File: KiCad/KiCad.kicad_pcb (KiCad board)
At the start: 2 copper layers, 26 parts, among them J1 DC-IN, J2 TYPE-C, SW1 TS665CJ, U1 ESP32-WROOM-32E, U2 MP1584EN, U3 CH340C, U4 RT9013-33GB

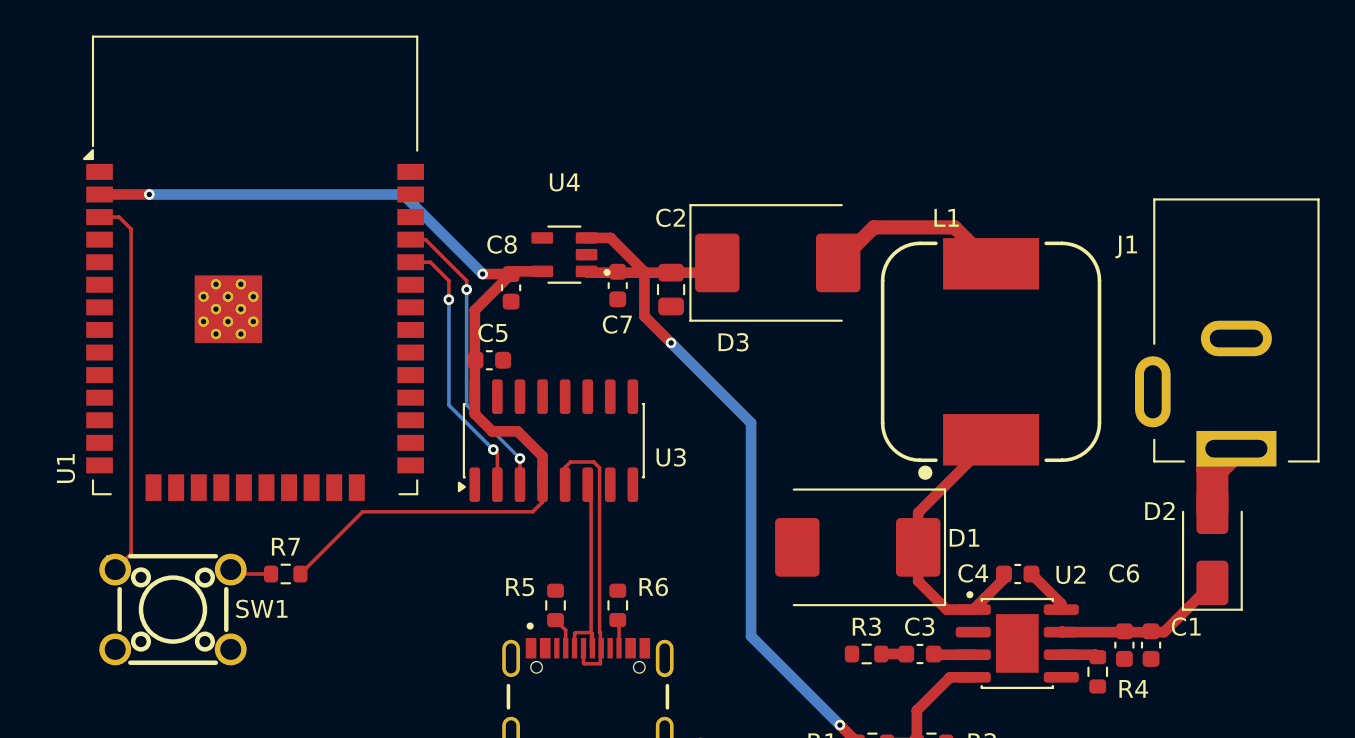
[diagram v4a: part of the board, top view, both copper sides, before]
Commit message: 完成esp32的燒錄/工作模式選擇電路之原理圖與PCB
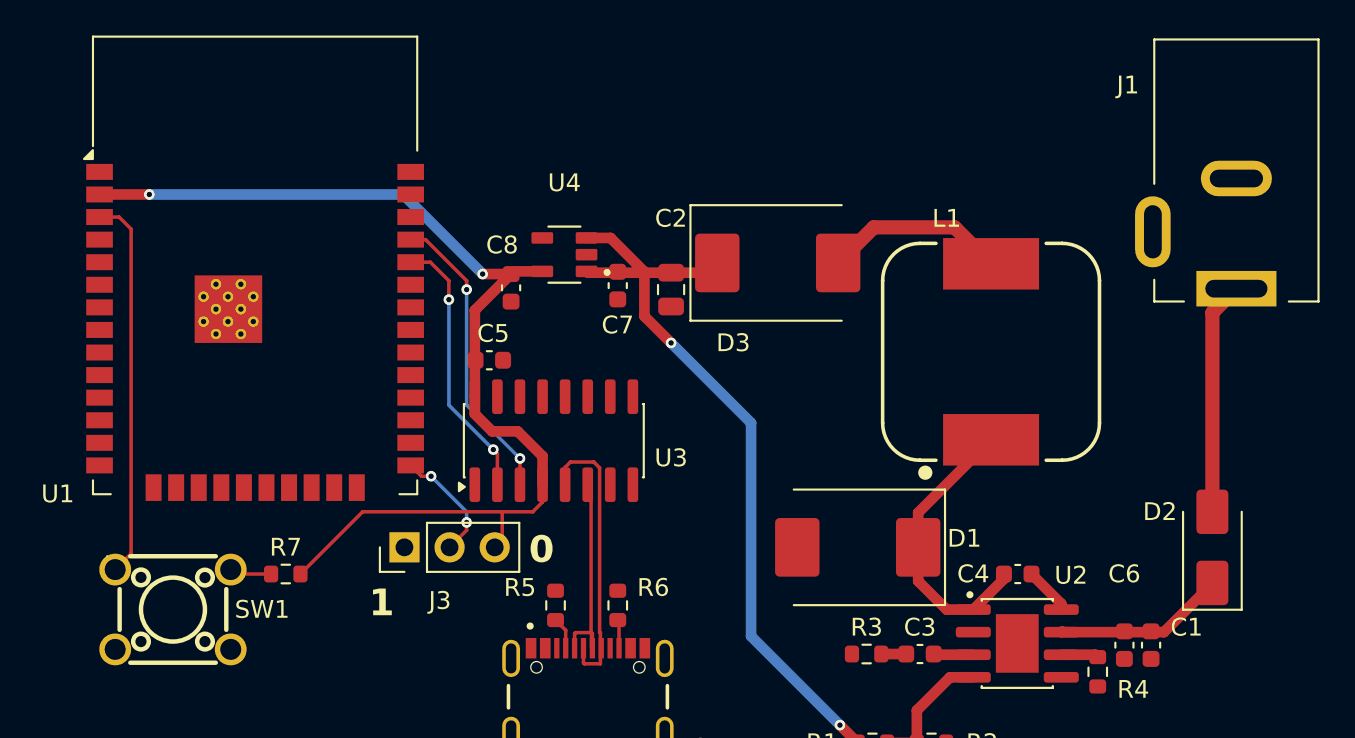
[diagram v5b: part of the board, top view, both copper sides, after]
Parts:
- added J3: Conn_01x03_Pin, Connector_PinHeader_2.54mm:PinHeader_1x03_P2.54mm_Vertical, F.Cu at (206.5, 89.0)
- moved J1 9.00 mm to (253.3, 74.5)
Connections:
- U1 pad 25: unconnected-(U1-IO0-Pad25) -> Net-(J3-Pin_2)
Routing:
- net VCC: track 4.56 -> 13.1 mm
- net Net-(J3-Pin_2): track 0.00 -> 6.63 mm, vias 0 -> 2
- net +3V3: track 57.9 -> 60.1 mm
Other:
- board text added: "0"
- board text added: "1"

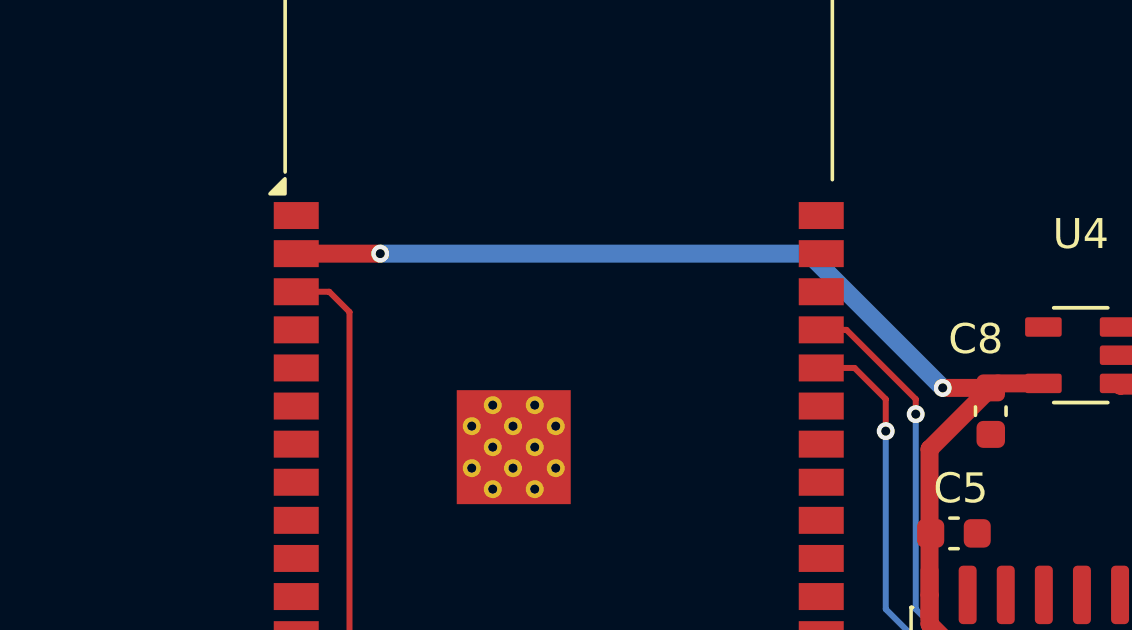
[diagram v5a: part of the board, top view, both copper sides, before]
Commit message: 補全mcu供電去偶電容
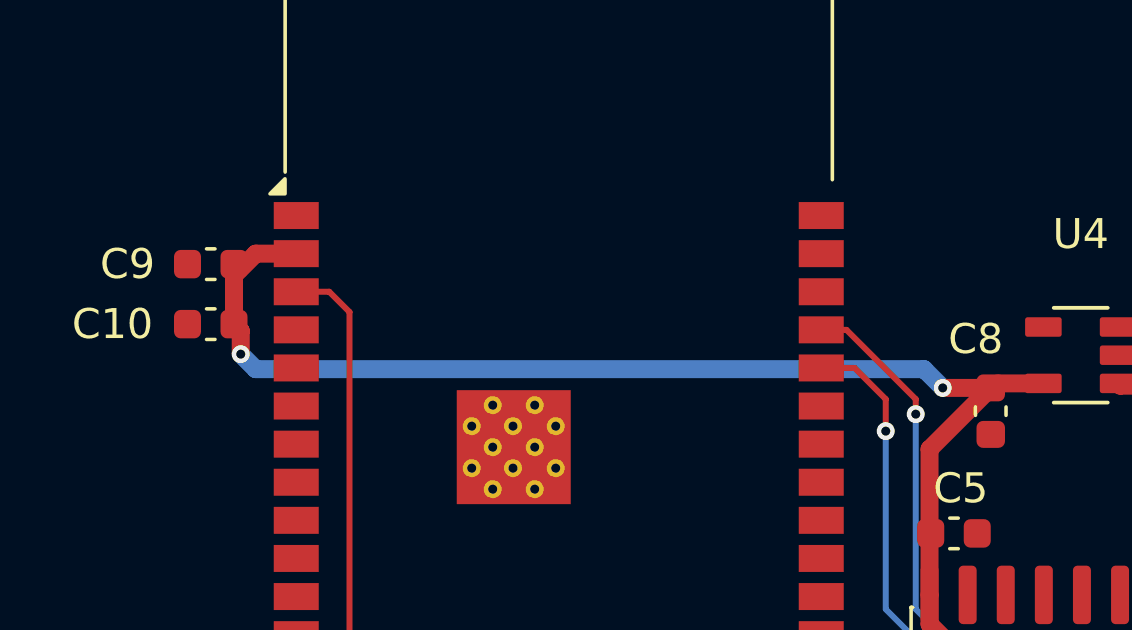
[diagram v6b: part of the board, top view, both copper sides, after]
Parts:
- added C10: 10uF, Capacitor_SMD:C_0603_1608Metric, F.Cu at (186.5, 71.5)
- added C9: 0.1uF, Capacitor_SMD:C_0603_1608Metric, F.Cu at (186.5, 69.5)
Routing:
- net +3V3: track 60.1 -> 65.6 mm

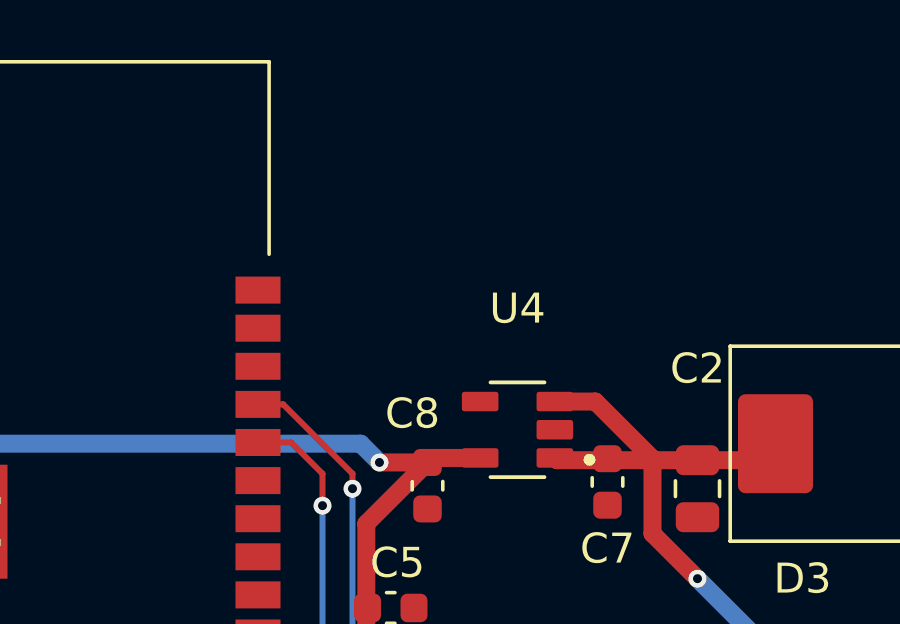
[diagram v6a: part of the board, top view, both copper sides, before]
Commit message: 放置0.96吋OLED
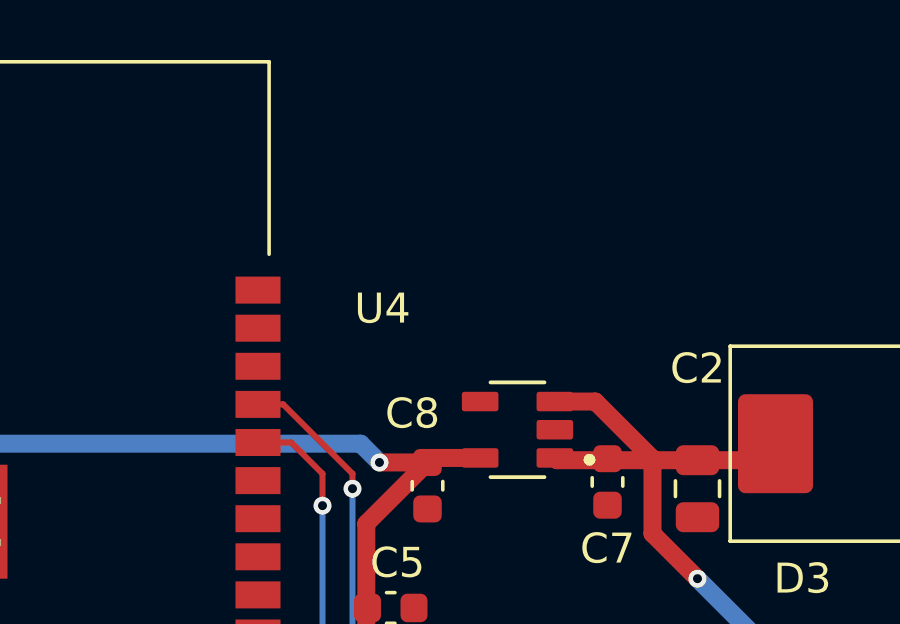
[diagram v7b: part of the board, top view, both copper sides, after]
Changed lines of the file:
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@@
 		(at 215.5 72.535001 180)
 		(property "Reference" "U4"
-			(at 0 4.035001 0)
+			(at 4.5 4.035001 0)
 			(layer "F.SilkS")
 			(effects

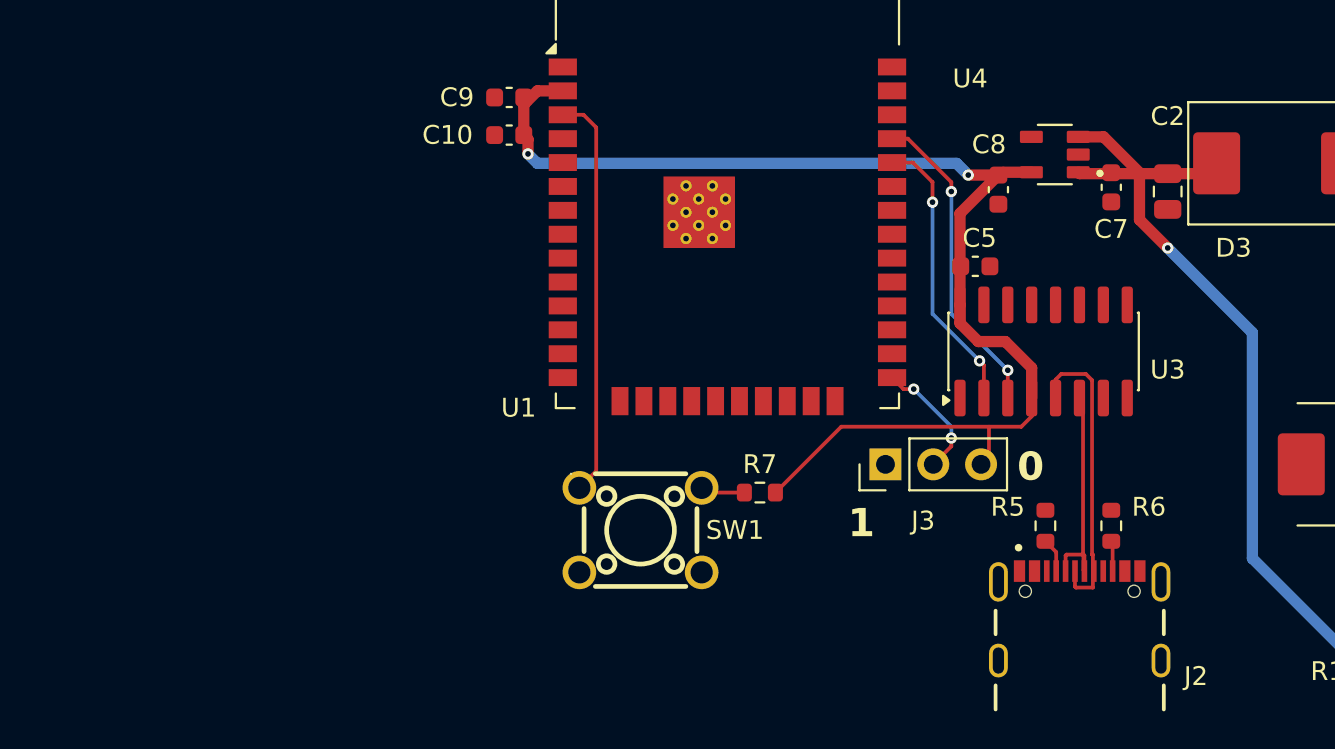
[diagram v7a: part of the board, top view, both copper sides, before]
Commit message: 增加0.96'OLED(已完成原理圖及PCB)及開始測試按鈕(只添加到PCB，原理圖未連接)
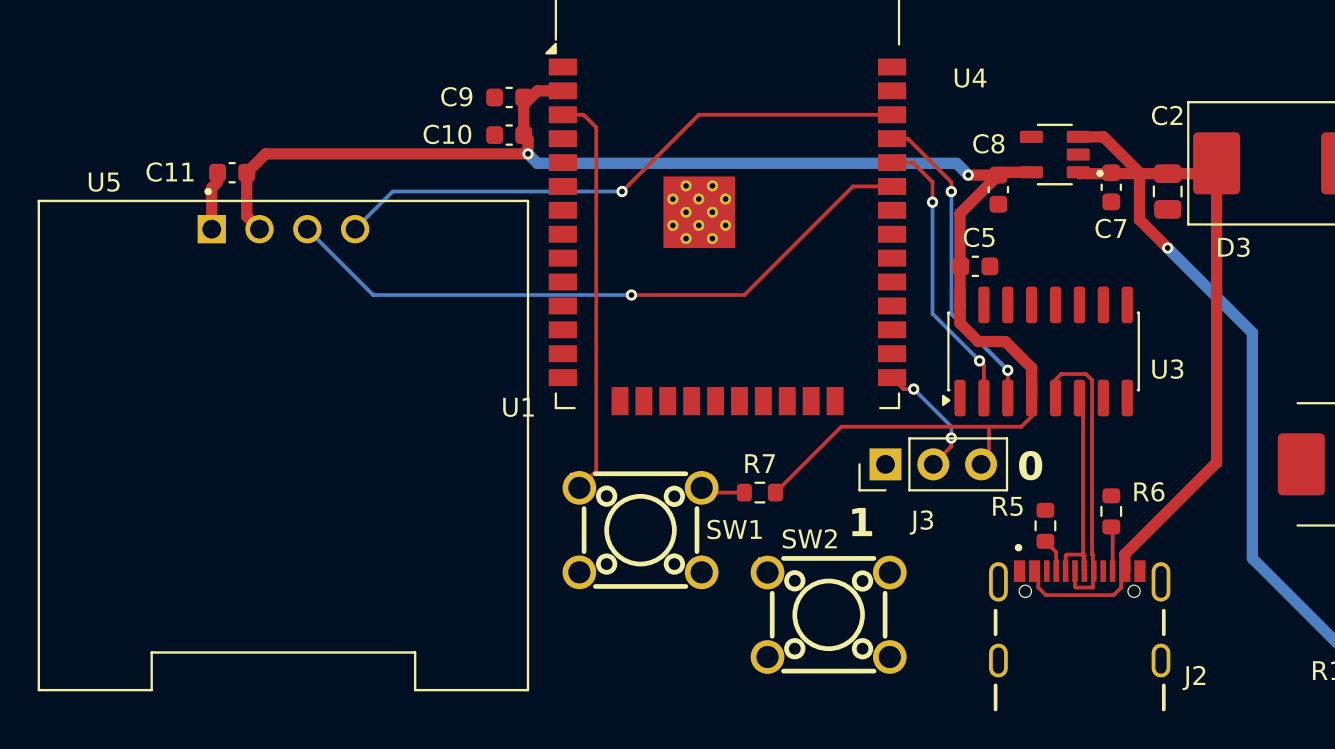
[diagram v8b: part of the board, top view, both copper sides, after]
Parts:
- added C11: 0.1uF, Capacitor_SMD:C_0603_1608Metric, F.Cu at (171.8, 73.5)
- added SW2: start, button:SW-TH_4P-L6.0-W6.0-P4.50-LS6.5, F.Cu at (203.5, 97.0)
- added U5: DM-OLED096-636, OLED:MODULE_DM-OLED096-636, F.Cu at (174.5, 88.0)
- SW1: value TS665CJ -> reset
- moved R6 0.77 mm to (218.5, 91.5)
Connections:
- U1 pad 33: unconnected-(U1-IO21-Pad33) -> /SDA
- U1 pad 36: unconnected-(U1-IO22-Pad36) -> /SCL
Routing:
- net /SDA: track 0.00 -> 34.9 mm, vias 0 -> 1
- net /SCL: track 0.00 -> 31.1 mm, vias 0 -> 1
- net +5V: track 43.2 -> 73.5 mm
- net +3V3: track 65.6 -> 84.3 mm
- net GND: track 0.06 -> 3.19 mm
- net Net-(J2-CC2): track 1.61 -> 2.38 mm
